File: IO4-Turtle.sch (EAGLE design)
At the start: 30 parts, among them CON2 RJ12/6, IC1 TC4428A, IC2 NE555S, Q1 PMBT2222, X1 0.156 Molex, X2 MSTBA5

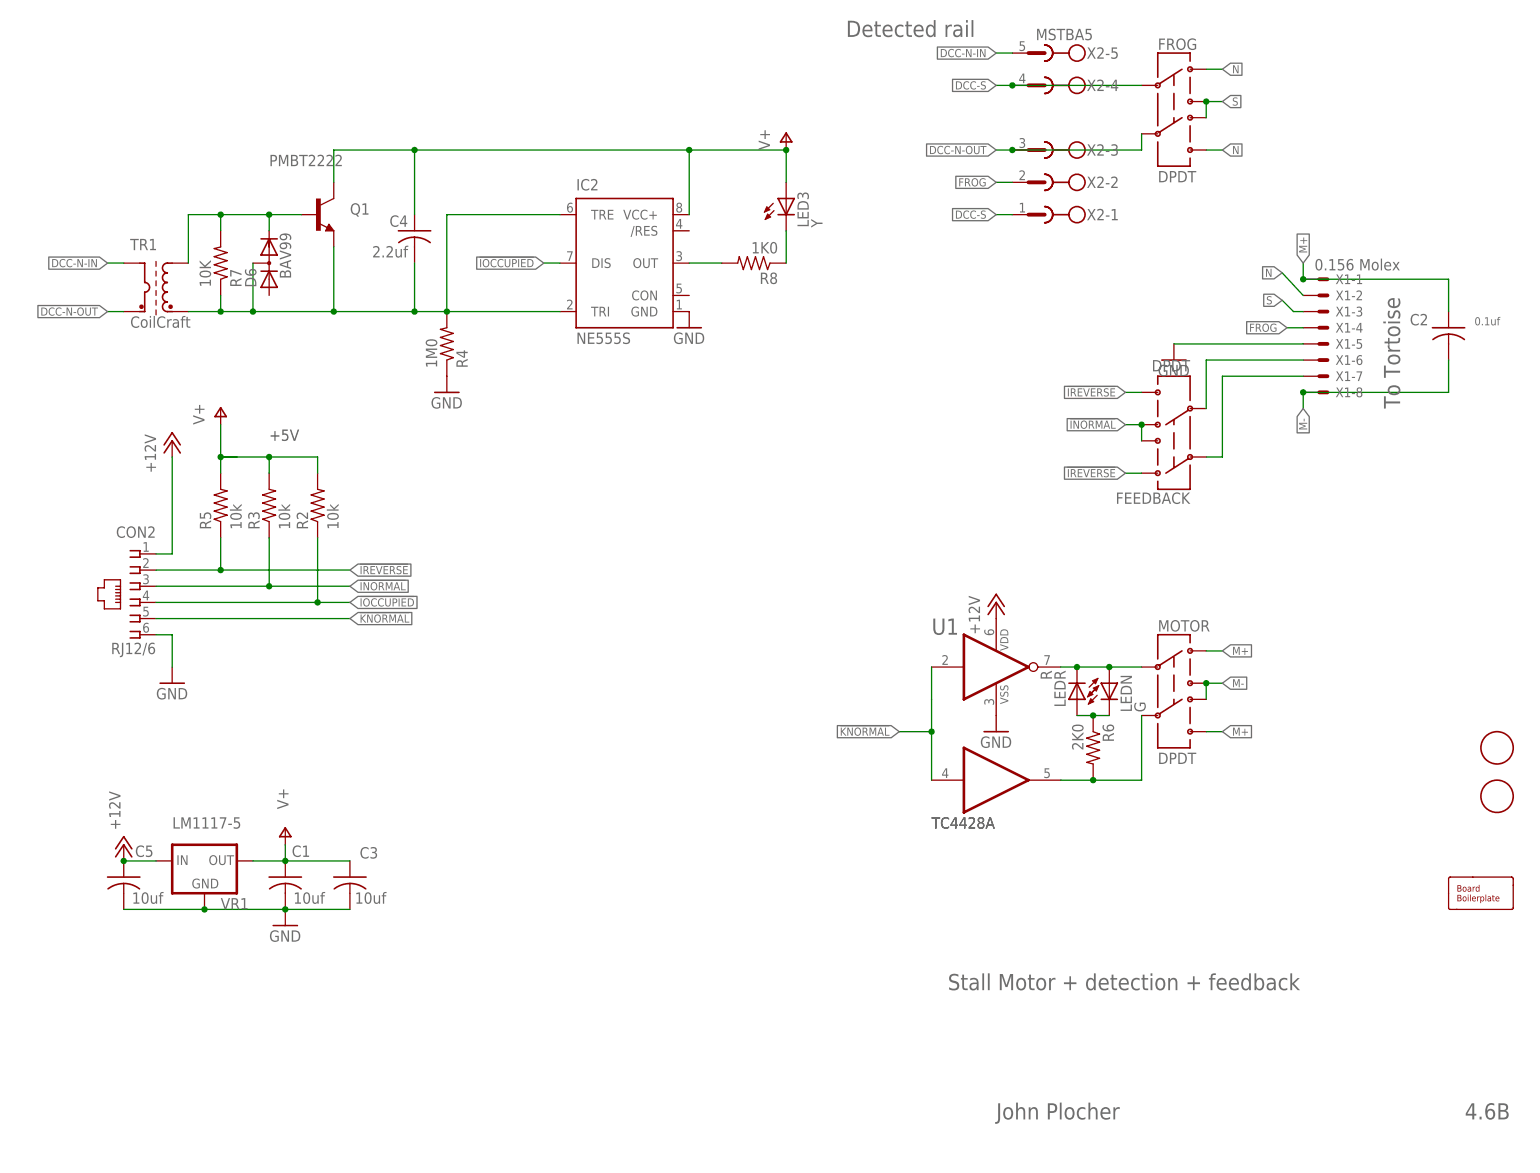
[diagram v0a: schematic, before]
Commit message: cleanup, replaced LM1117 output cap
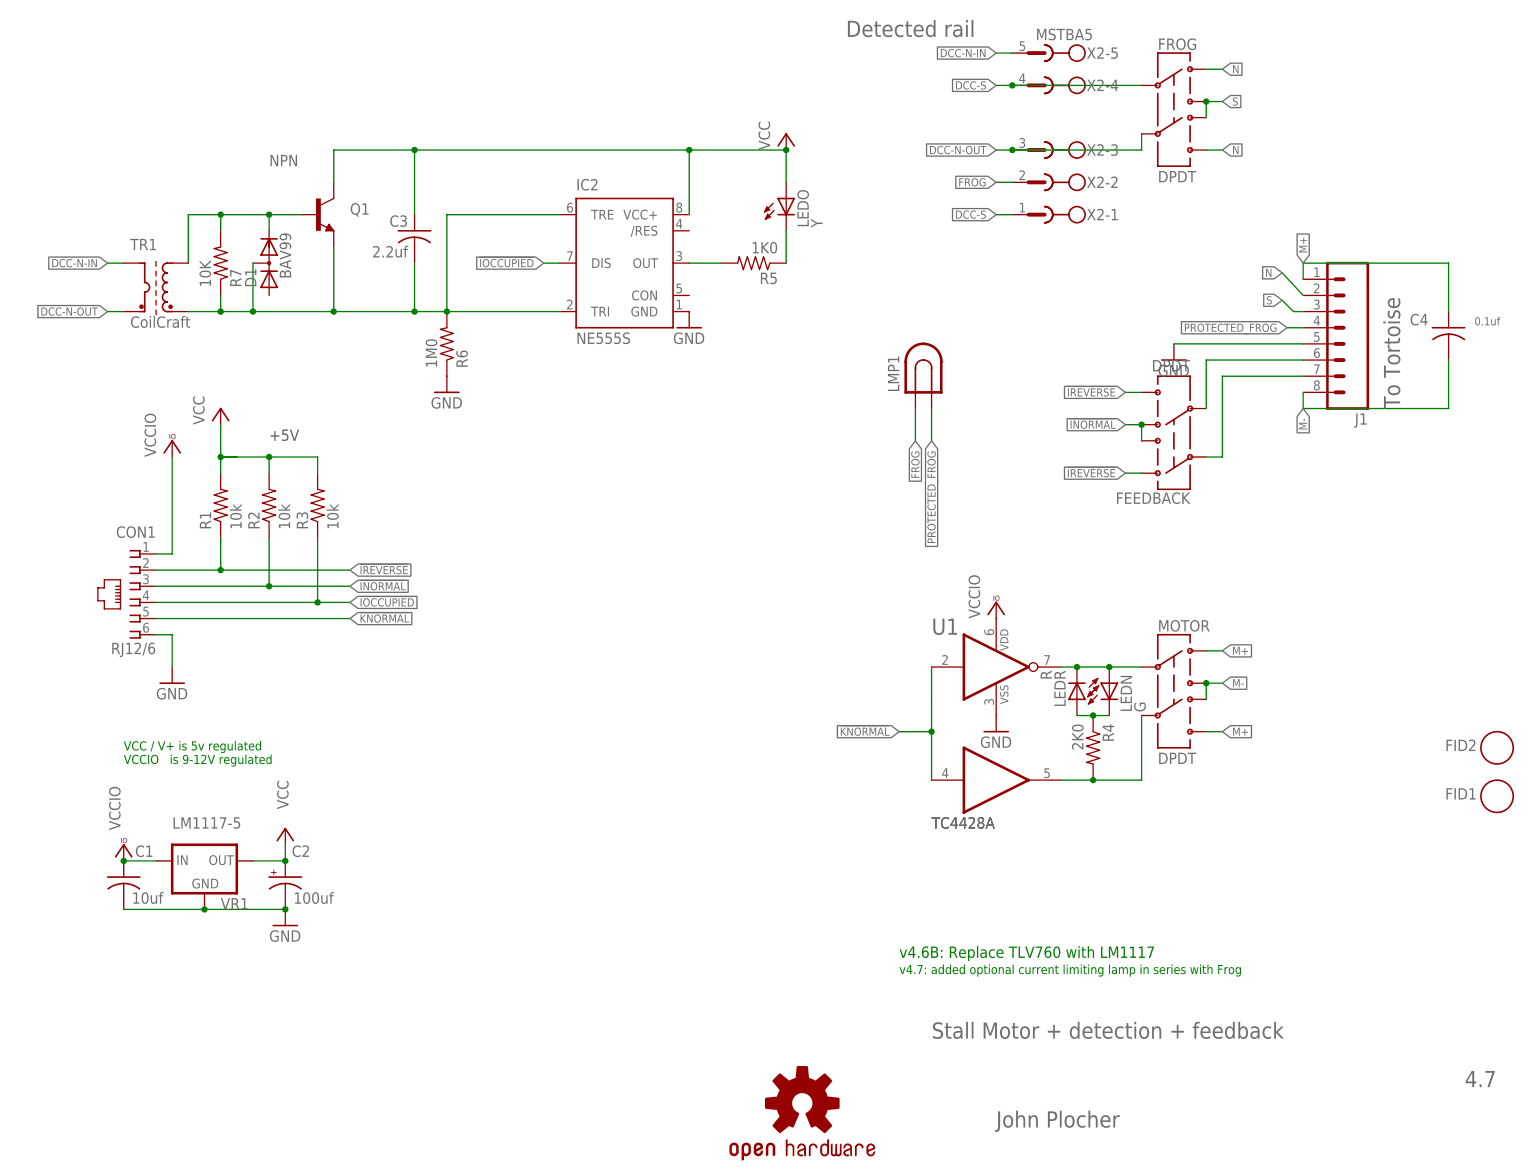
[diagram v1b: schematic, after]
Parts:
- removed BOARD: BOARD70X50-HOHOLES, SPCoast:BOARD50X70-TEMPLATE
- removed C5: 10uf, SPCoast:CAP0805
- removed R8: 1K0, SPCoast:R0805-RES
- removed X1: 0.156 Molex, SPCoast:KK-156-8F
- added J1: (no value), SPCoast:CONNECTOR-M081.56-F
- added LMP1: (no value), SPCoast:LAMPBULB
- added OSHW1: DOC-OSHW-LOGO-M, SPCoast:DOC-OSHW-LOGO-M
- added R1: 10k, SPCoast:R0805-RES
- C2: value 0.1uf -> 100uf; device SPCoast:CAP0805 -> SPCoast:CAP-POLD
- C3: value 10uf -> 2.2uf
- C4: value 2.2uf -> 0.1uf
- IC1: device tc442xa:TC4428ACOASOIC -> SPCoast:TC4428ACOASOIC
- Q1: value PMBT2222 -> NPN
- R4: value 1M0 -> 2K0
- R5: value 10k -> 1K0
- R6: value 2K0 -> 1M0
- renumbered CON2 to CON1, D6 to D1, LED3 to LEDO
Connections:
- new net PROTECTED_FROG: J1.4, LMP1.2
- net !INORMAL: now also R2.1; no longer R3.1
- net !IOCCUPIED: now also R3.1; no longer R2.1
- net !IREVERSE: now also R1.1; no longer R5.1
- net +12V: now also C1.1; no longer C5.1
- net FROG: now also LMP1.1; no longer X1-4.S
- net GND: now also C2.-, J1.5, R6.1; no longer C3.2, C5.2, R4.1, X1-5.S
- net M+: now also C4.1, J1.1; no longer C2.1, X1-1.S
- net M-: now also C4.2, J1.8; no longer C2.2, X1-8.S
- net N: now also J1.2; no longer X1-2.S
- net N$16: now also J1.6; no longer X1-6.S
- net N$17: now also J1.7; no longer X1-7.S
- net N$19: now also R4.2; no longer R6.2
- net N$3: now also R4.1; no longer R6.1
- net N$8: now also R5.1; no longer R8.1
- net N$9: now also R5.2; no longer R8.2
- net S: now also J1.3; no longer X1-3.S
- net TRIGGER: now also C3.2, R6.2; no longer C4.2, R4.2
- net V+: now also C2.+, R1.2; no longer C1.1, C4.1, R5.2
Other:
- note added: "4.7"
- note added: "VCC / V+ is 5v regulated VCCIO is 9-12V regulated"
- note added: "v4.6B: Replace TLV760 with LM1117"
- note added: "v4.7: added optional current limiting lamp in series with Frog"
- note removed: "4.6B"
- note removed: "Replace TLV760 with LM1117"
- moved on the sheet: C1, C3, C4, R2, R3, R4, R5, R6
